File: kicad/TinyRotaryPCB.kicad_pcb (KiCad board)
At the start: 2 copper layers, 23 x 15 mm, 5 parts, among them J1 Conn_01x05_Pin, SW1 RotaryEncoder_Switch

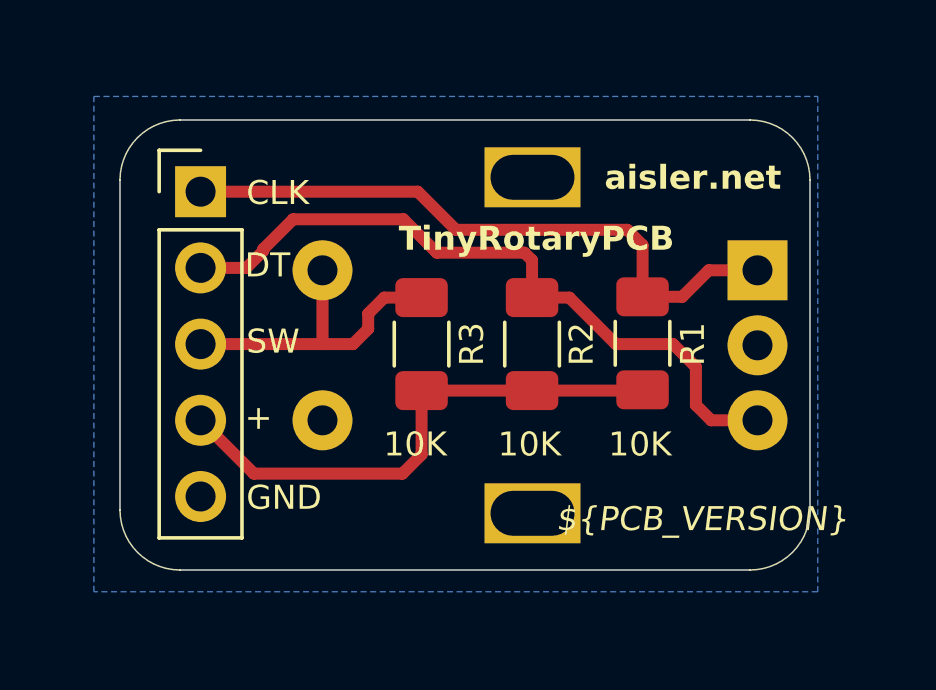
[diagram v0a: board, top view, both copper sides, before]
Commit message: Update KiCad project, horizontal pin header
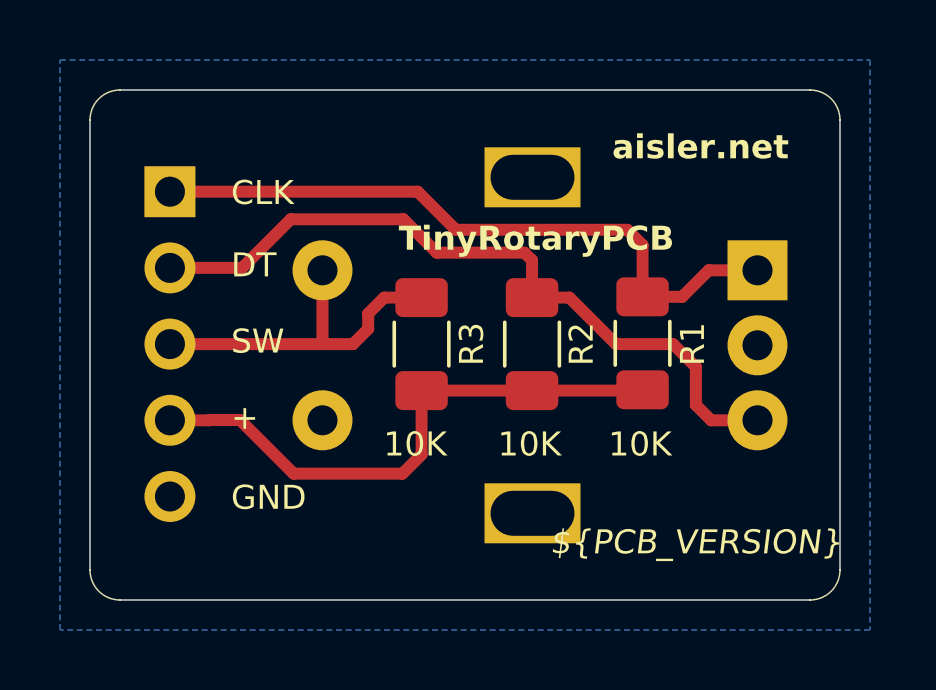
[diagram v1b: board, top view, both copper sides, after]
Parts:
- J1: footprint Connector_PinHeader_2.54mm:PinHeader_1x05_P2.54mm_Vertical -> PinHeader_1x05_P2.54mm_H_W_S:PinHeader_1x05_P2.54mm_Horizontal_Without_Silkscreen; moved to B.Cu
- moved J1 1.02 mm to (153.7, 72.4), turned to 180 degrees
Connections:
- SW1 pad MP: GND -> (no net)
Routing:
- net VCC: track 17.8 -> 18.9 mm
- net /SW: track 10.8 -> 11.8 mm
- net /CLK: track 21.4 -> 22.4 mm
- net /DT: track 23.5 -> 24.5 mm
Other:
- board size 23 x 15 mm -> 25 x 17 mm
